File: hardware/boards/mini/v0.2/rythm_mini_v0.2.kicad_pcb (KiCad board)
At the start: 8 copper layers, 20 x 41 mm, 96 parts, among them IC1 NAU88C22YG, IC3 IS42S16160J-6BLI, J2 Top, J3 Bottom, Q1 PMV37EN22, U1 W25Q128JVP, U2 LTV-217-G, U4 STM32H750XBHx, Y1 Crystal_GND24

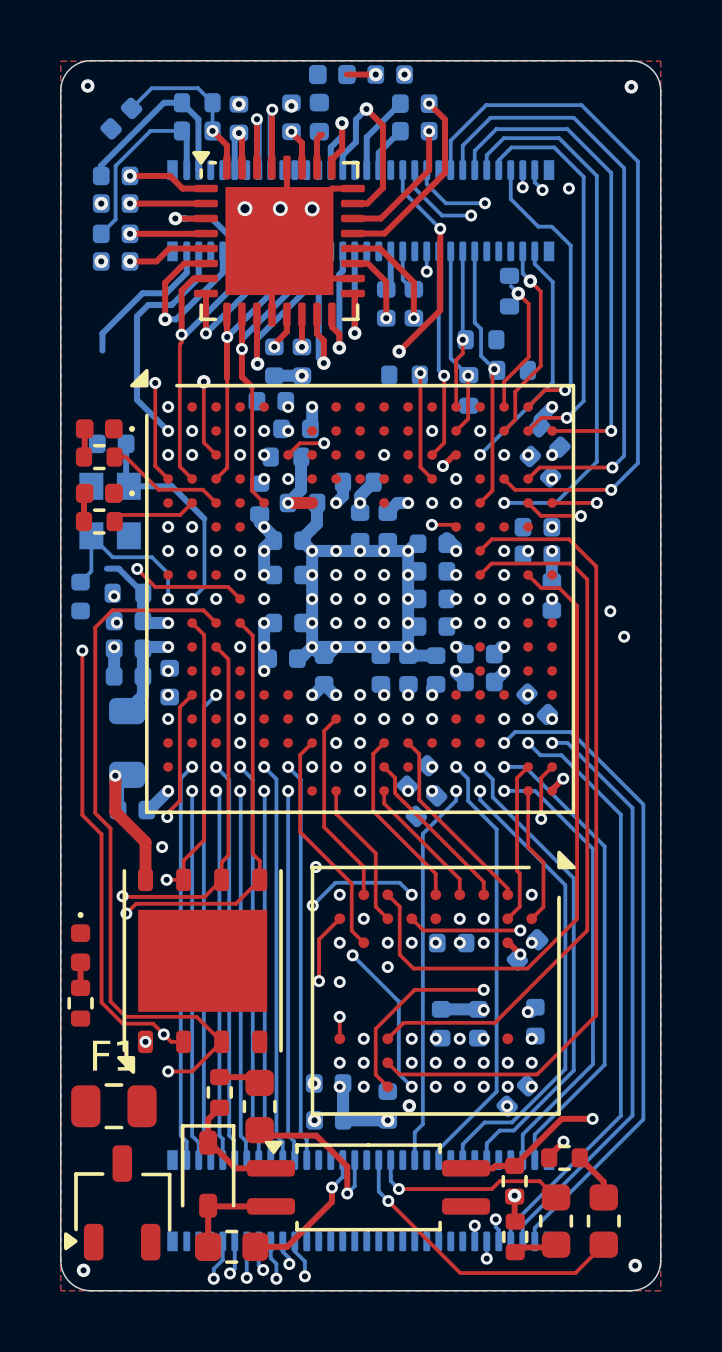
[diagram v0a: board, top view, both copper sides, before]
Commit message: mini: more GPIO routing, added OSC32 oscillator
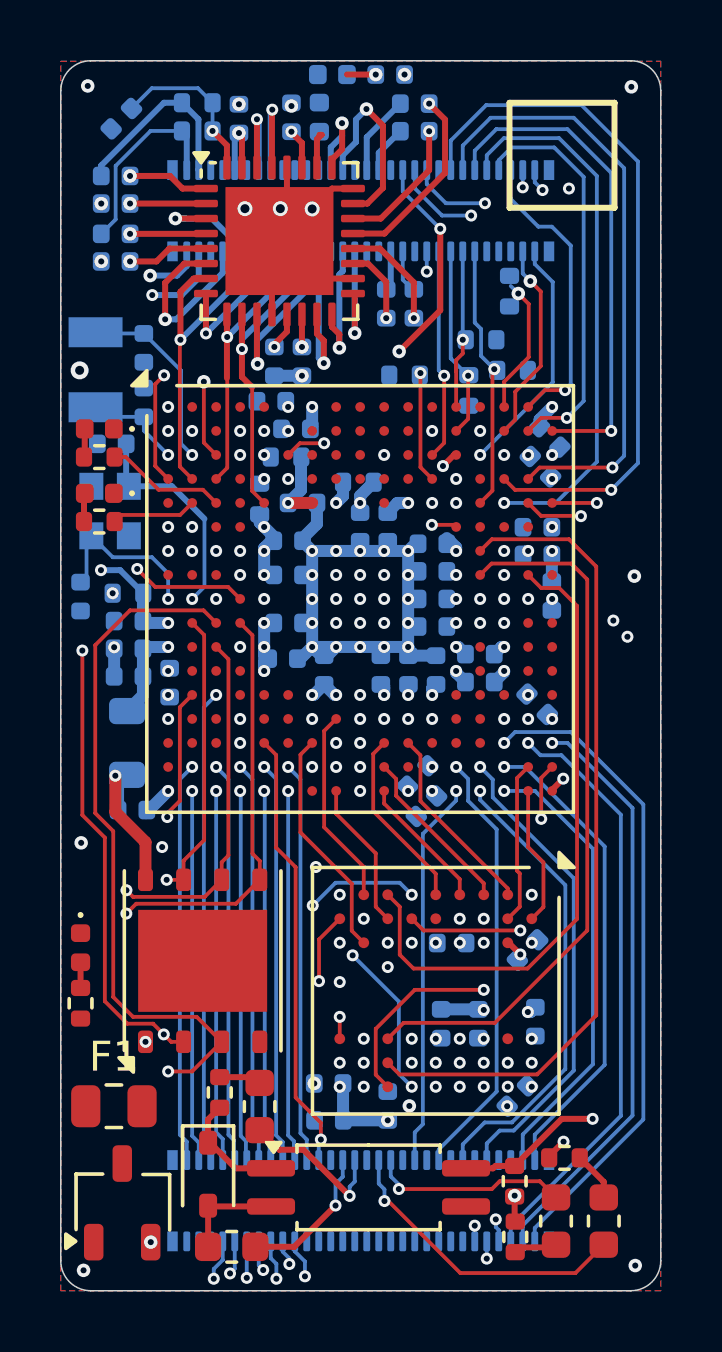
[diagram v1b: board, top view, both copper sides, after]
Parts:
- added C39: C, Capacitor_SMD:C_0402_1005Metric, B.Cu at (72.8, 66.6)
- added C40: C, Capacitor_SMD:C_0402_1005Metric, B.Cu at (72.8, 68.4)
- added REF**: OSHW-Symbol_6.7x6mm_SilkScreen, Symbol:OSHW-Symbol_6.7x6mm_SilkScreen, B.Cu at (77.3, 81.5)
- added Y3: Crystal, Crystal:Crystal_SMD_3215-2Pin_3.2x1.5mm, B.Cu at (71.2, 67.3)
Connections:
- J3 pad 37: unconnected-(J3-Pad37) -> /PA7
- U4 pad C1: unconnected-(U4C-PC15-PadC1) -> /OSC32_OUT
- U4 pad C2: unconnected-(U4C-PC14-PadC2) -> /OSC32_IN
- U4 pad R5: unconnected-(U4A-PA7-PadR5) -> /PA7
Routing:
- net /PA7: track 0.00 -> 14.7 mm, vias 0 -> 1
- net /RST: track 8.27 -> 15.9 mm, vias 1 -> 3
- net /OSC32_IN: track 0.00 -> 6.34 mm, vias 0 -> 1
- net /OSC32_OUT: track 0.00 -> 3.35 mm, vias 0 -> 1
- net /VBAT: track 7.73 -> 7.84 mm, vias 1 -> 2
- net unconnected-(U4C-PC15-PadC1): vias 1 -> 0
- net unconnected-(U4C-PC14-PadC2): vias 1 -> 0
- net GND: vias 77 -> 79
